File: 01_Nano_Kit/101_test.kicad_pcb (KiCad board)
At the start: 4 copper layers, 78.8 x 54.2 mm, 46 parts, among them J11 Conn_02x02_Counter_Clockwise, J12 Conn_02x02_Counter_Clockwise, J14 Conn_01x08, J15 Conn_02x02_Counter_Clockwise, Q1 BC817, SW1 SW_Push, SW3 A4 | SDA, SW4 A5 | SCL, SW5 A0 | GPIO IN, U1 LM2596S-5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

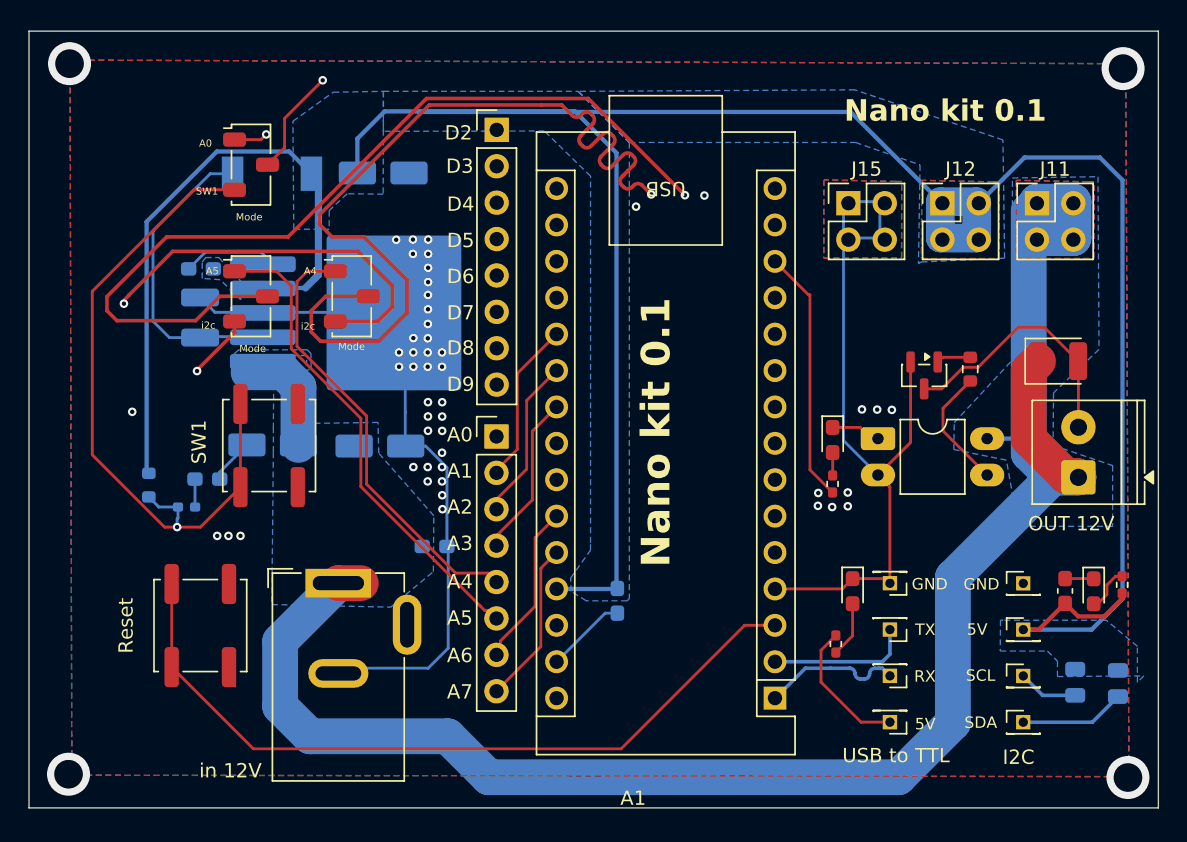
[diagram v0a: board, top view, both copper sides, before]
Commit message: Update PCB layout: Add copper zone and fix DRC warning
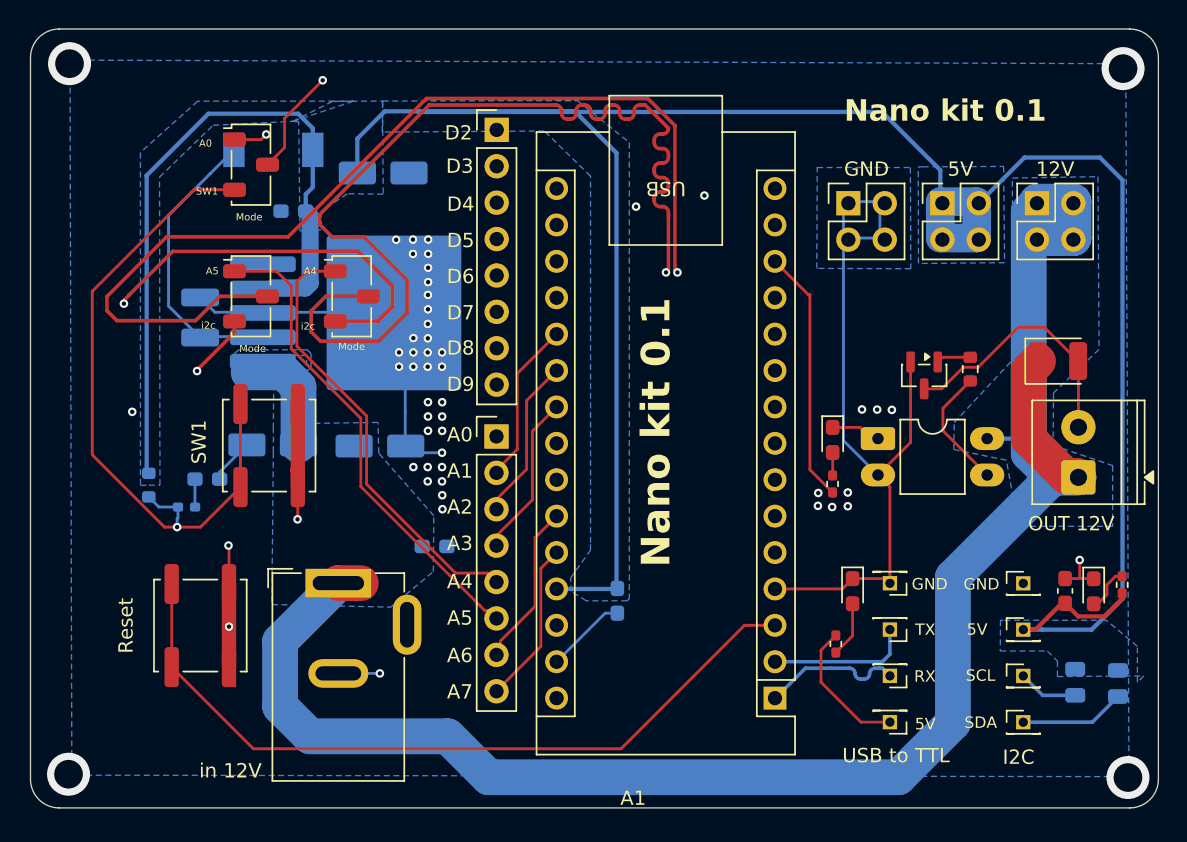
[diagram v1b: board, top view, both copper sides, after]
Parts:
- moved C6 7.60 mm to (123.5, 88.0)
- moved L1 1.67 mm to (122.1, 83.7)
- renumbered J11 to 12V, J12 to 5V, J15 to GND
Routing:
- net I2C_-: track 120.7 -> 97.6 mm
- net +5V: track 206.9 -> 214.6 mm
- net GND: track 117.9 -> 112.4 mm, vias 48 -> 50
- net /i2c-: track 85.6 -> 89.0 mm
- net /i2c+: track 85.4 -> 88.6 mm
- net Net-(D1-K): track 22.3 -> 21.0 mm
- removed copper zone on F.Cu, net +12V
- removed copper zone on In1.Cu, net +12V
- removed copper zone on In2.Cu, net +12V
- removed copper zone on F.Cu, net +5V
- removed copper zone on In1.Cu, net +5V
- removed copper zone on In2.Cu, net +5V
- removed copper zone on F.Cu, net GND
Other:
- board size 78.8 x 54.2 mm -> 78.7 x 54.4 mm
